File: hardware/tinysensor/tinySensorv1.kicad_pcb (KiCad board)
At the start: 2 copper layers, 97.9 x 63.8 mm, 40 parts, among them J1 RADIO, J10 CR2032 socket, J11 AAA socket, J12 AA Socket, J13 RAW IN, J2 DCDC converter, J3 I2C Sensor (BME/BMP 280), J4 Digital out, J5 OneWire sensor, J6 ISP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

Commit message: hardware: Update of Kikad design, new batch expected
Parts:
- removed J11: AAA socket, Battery:BatteryHolder_Keystone_2466_1xAAA
- removed J12: AA Socket, Battery:BatteryHolder_Keystone_2460_1xAA
- removed R5: 10k, Resistor_THT:R_Axial_DIN0204_L3.6mm_D1.6mm_P7.62mm_Horizontal
- removed REF**: BatteryHolder_MPD_BH-18650-PC2, Battery:BatteryHolder_MPD_BH-18650-PC2
- added 18650: BatteryHolder_MPD_BH-18650-PC2, Battery:BatteryHolder_MPD_BH-18650-PC2, B.Cu at (124.0, 98.6)
- R2, R3: moved to B.Cu
- moved MH2 49.2 mm to (117.6, 105.4)
- moved R1 18.8 mm to (162.1, 84.6), turned to 90 degrees
- moved SW1 13.6 mm to (153.5, 68.1), turned to 0 degrees
- moved D1 11.6 mm to (158.0, 81.6), turned to 90 degrees
- moved MH5 9.71 mm to (150.9, 51.8)
- moved J10 3.26 mm to (130.1, 82.6)
- moved C6 1.67 mm to (164.1, 54.6)
- moved JP1 0.88 mm to (171.2, 73.7)
- moved J2 0.07 mm to (147.6, 58.8)
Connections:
- D1 pad 1: (no net) -> Net-(D1-K)
- R1 pad 1: Net-(D1-Pad1) -> Net-(D1-K)
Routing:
- net /RESET: track 54.9 -> 40.2 mm
- net Net-(D1-K): track 0.00 -> 6.07 mm
- net Net-(D1-Pad1): track 5.68 -> 0.00 mm
- net VCC: track 92.2 -> 87.3 mm
- net +BATT: track 127.7 -> 131.9 mm
- net GND: track 9.87 -> 13.8 mm
- net Net-(J7-Pin_3): track 14.5 -> 16.1 mm
- net /SENSOR_VCC: track 72.7 -> 74.4 mm
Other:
- board size 97.9 x 63.8 mm -> 94 x 63.8 mm
- board text added: "GND"
- board text added: "S. VCC"
- board text added: "SCL"
- board text added: "SDA"
- board text removed: "Direct Vcc"
- board text removed: "gnd"
- board text removed: "scl"
- board text removed: "sda"
- board text removed: "sensor Vcc"

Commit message: hardware: Better ground plane
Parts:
- removed 18650: BatteryHolder_MPD_BH-18650-PC2, Battery:BatteryHolder_MPD_BH-18650-PC2
- added JP5: , Jumper:SolderJumper-2_P1.3mm_Open_TrianglePad1.0x1.5mm, B.Cu at (166.1, 61.2)
- added REF**: BatteryHolder_MPD_BH-18650-PC2, Battery:BatteryHolder_MPD_BH-18650-PC2, F.Cu at (124.7, 99.1)
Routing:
- net +BATT: track 131.9 -> 123.7 mm, vias 2 -> 1
- net VCC: track 87.3 -> 80.7 mm
- net GND: track 13.8 -> 17.0 mm

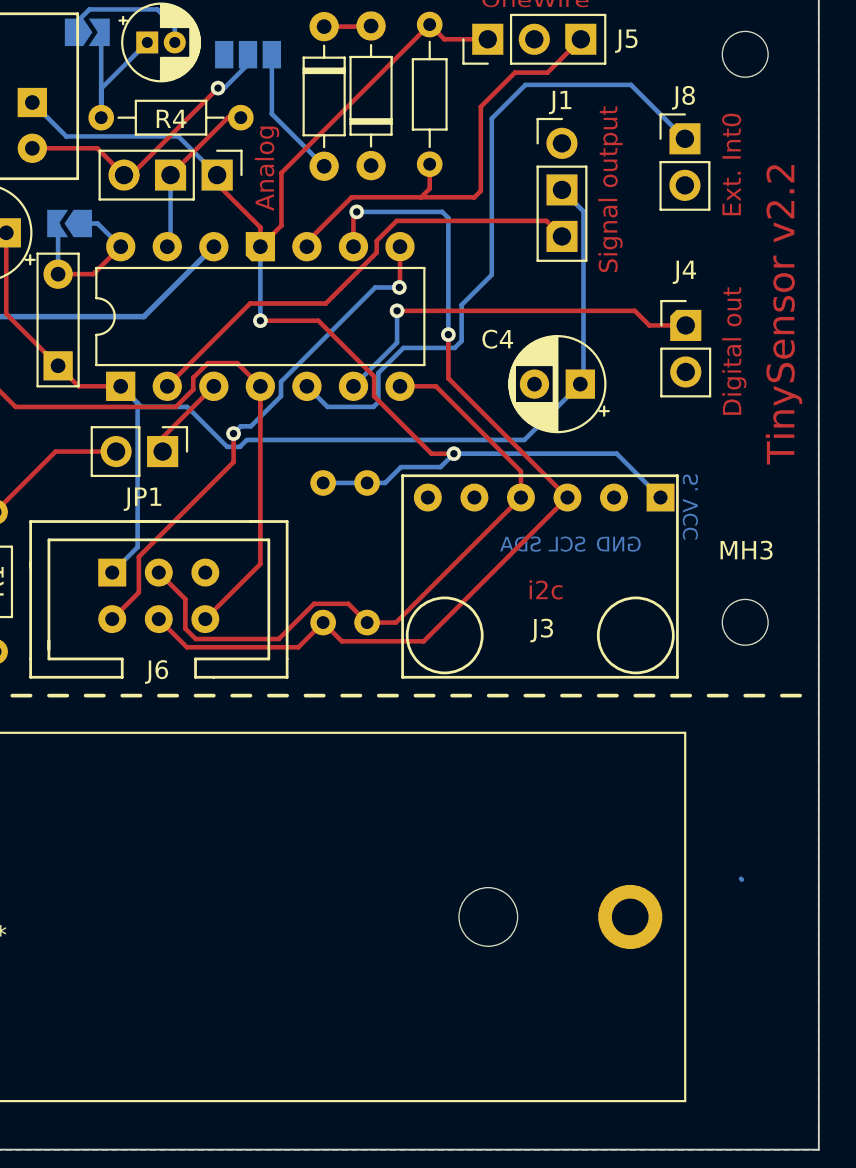
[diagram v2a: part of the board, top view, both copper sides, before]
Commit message: hardware: double I²C connector
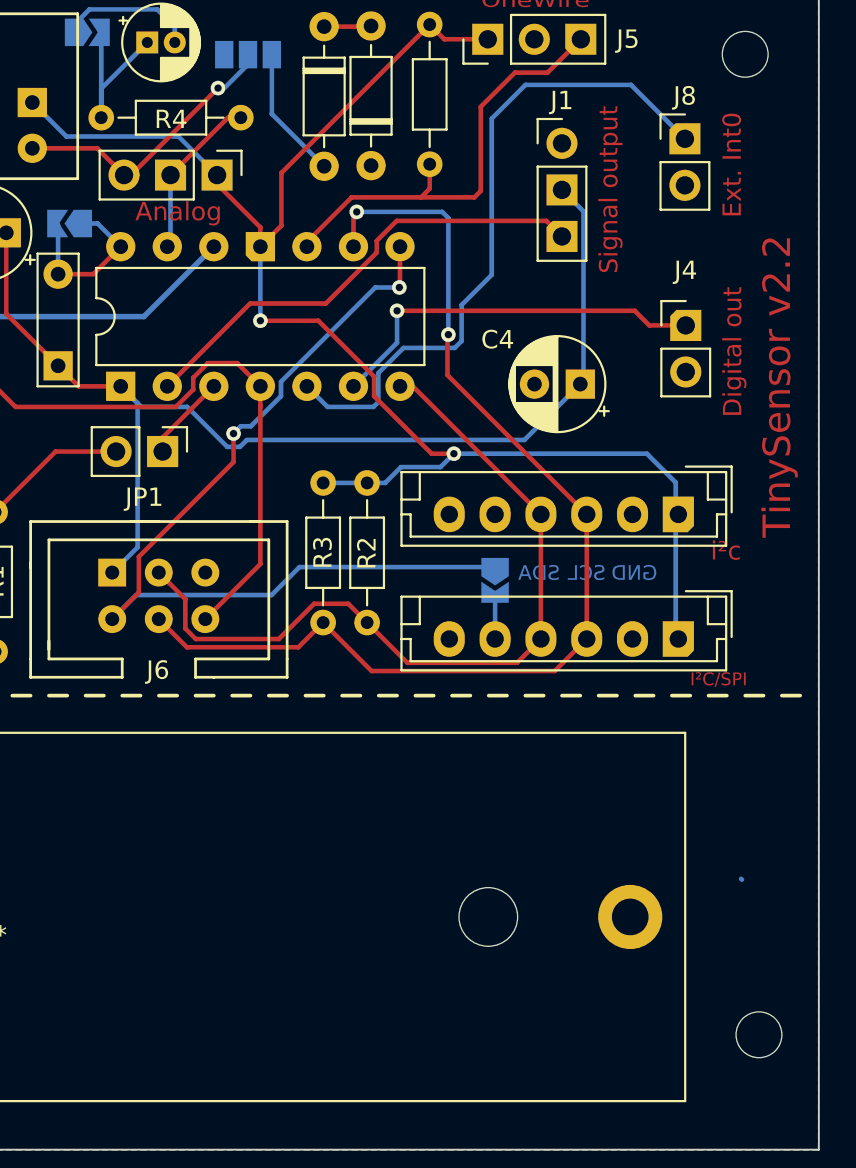
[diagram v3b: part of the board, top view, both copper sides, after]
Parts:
- removed J3: I2C Sensor (BME/BMP 280), TinySensor lib:BMx280_breakout
- removed MH3: MountingHole, MountingHole:MountingHole_2.5mm
- added I2C: JST_EH_B6B-EH-A_1x06_P2.50mm_Vertical, Connector_JST:JST_EH_B6B-EH-A_1x06_P2.50mm_Vertical, F.Cu at (199.4, 77.1)
- added I2C_SPI: JST_EH_B6B-EH-A_1x06_P2.50mm_Vertical, Connector_JST:JST_EH_B6B-EH-A_1x06_P2.50mm_Vertical, F.Cu at (199.4, 83.9)
- added JP6: DIRECT Vcc, Jumper:SolderJumper-2_P1.3mm_Open_TrianglePad1.0x1.5mm, B.Cu at (189.4, 80.7)
- added MH1: MountingHole, MountingHole:MountingHole_2.5mm, F.Cu at (203.8, 105.5)
- R2, R3: moved to F.Cu
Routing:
- net /MISO: track 27.9 -> 52.5 mm
- net /SENSOR_VCC: track 74.4 -> 83.5 mm
- net /SCL: track 52.2 -> 59.6 mm
- net /SDA: track 36.2 -> 43.4 mm
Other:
- board text added: "I²C/SPI"
- board text added: "i²c"
- board text removed: "S. VCC"
- board text removed: "i2c"
